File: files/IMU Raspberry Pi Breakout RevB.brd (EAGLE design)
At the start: 65 x 56 mm, 13 parts, among them J1 PIN20X2, J2 ADIS1648X/49X/54X, J4 455-1750-1-ND, U1 ADM7172ACPZ-3.3-R7

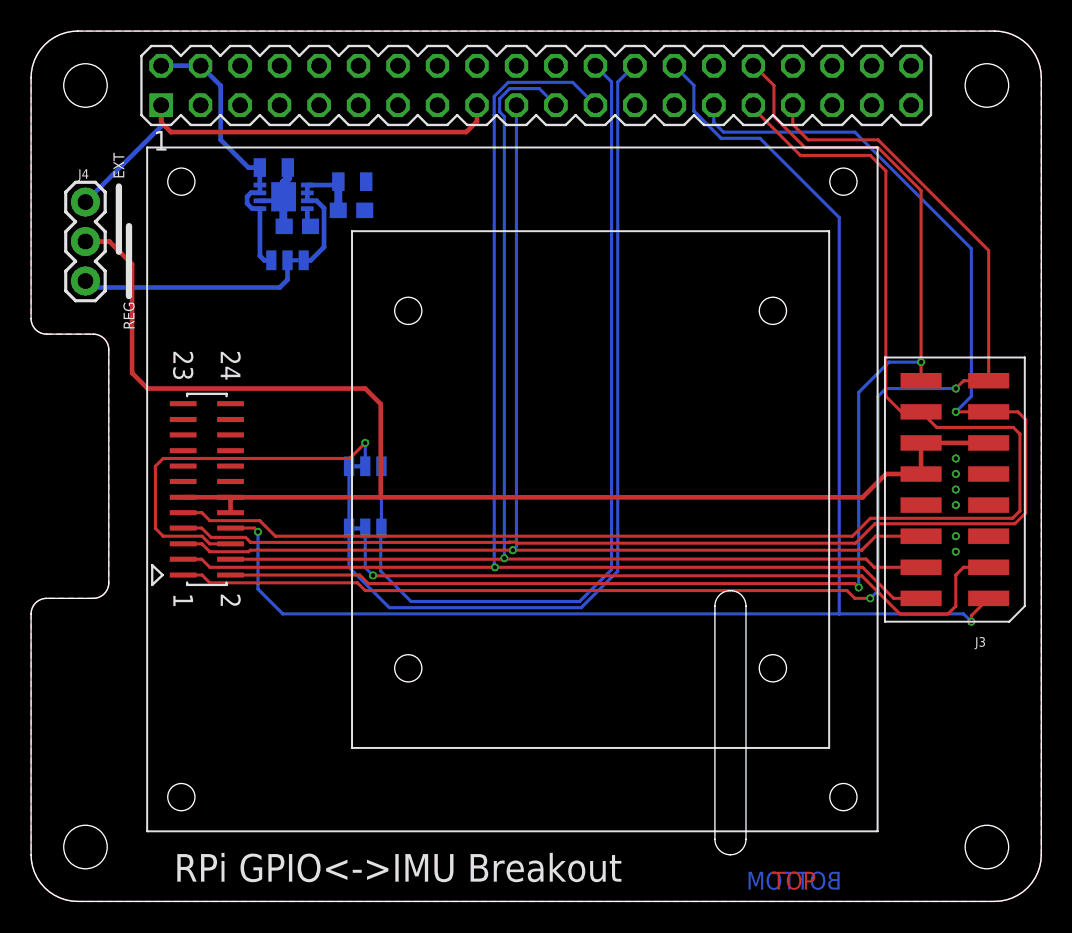
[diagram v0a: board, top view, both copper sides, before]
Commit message: Updated design to include resistors that link SPI1 to SPI0. Improved silkscreen art.
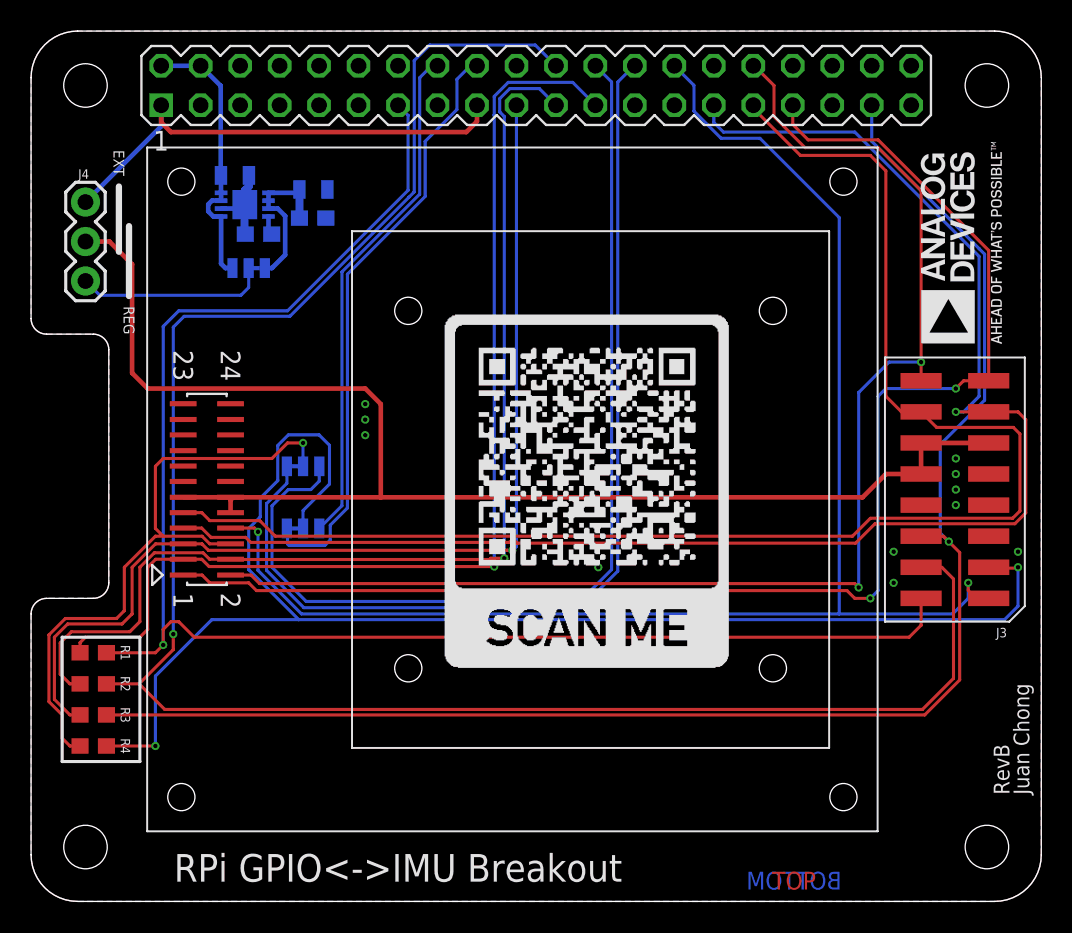
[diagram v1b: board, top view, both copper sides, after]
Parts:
- added R1, R2, R3, R4: 0, SparkFun-Resistors:0603
- moved JP1 4.00 mm to (17.5, 28.0)
- moved JP2 4.00 mm to (17.5, 24.0)
- moved U1 2.55 mm to (13.7, 44.8)
- moved C1 2.55 mm to (13.1, 46.7)
- moved C2 2.55 mm to (18.2, 45.8)
- moved C4 2.55 mm to (18.1, 44.0)
- moved JP3 2.55 mm to (14.0, 40.8)
- moved C3 2.55 mm to (14.6, 42.9)
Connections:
- removed net MISO: J1.21, J2.4, J3.4
- removed net MOSI: J1.19, J2.5, J3.6
- removed net N$2: J1.26, JP1.3, JP2.3
- removed net N$3: J1.24, JP1.1, JP2.1
- removed net SCLK: J1.23, J2.3, J3.2
- new net SPI0_CS0: J1.24, JP1.1
- new net SPI0_CS1: J1.26, JP1.3
- new net SPI0_MISO: J1.21, J2.4, R2.2
- new net SPI0_MOSI: J1.19, J2.5, R3.2
- new net SPI0_SCLK: J1.23, J2.3, R1.2
- new net SPI1_CS0: J1.18, JP2.3
- new net SPI1_CS1: J1.16, JP2.1
- new net SPI1_MISO: J1.22, J3.4, R2.1
- new net SPI1_MOSI: J1.37, J3.6, R3.1
- new net SPI1_SCLK: J1.13, J3.2, R1.1
- net !CS_1MM: now also R4.2
- net !CS_2MM: now also R4.1
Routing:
- net SPI1_MISO: track 0.00 -> 126.3 mm, vias 0 -> 1
- net SPI1_SCLK: track 0.00 -> 101.9 mm, vias 0 -> 1
- net SPI1_MOSI: track 0.00 -> 99.4 mm, vias 0 -> 1
- net SCLK: track 86.3 -> 0.00 mm, vias 1 -> 0
- net MISO: track 78.7 -> 0.00 mm, vias 1 -> 0
- net MOSI: track 76.8 -> 0.00 mm, vias 1 -> 0
- net SPI0_MISO: track 0.00 -> 70.8 mm, vias 0 -> 1
- net SPI0_SCLK: track 0.00 -> 69.8 mm, vias 0 -> 1
- net SPI0_MOSI: track 0.00 -> 68.7 mm, vias 0 -> 1
- net SPI0_CS0: track 0.00 -> 65.1 mm
- net SPI0_CS1: track 0.00 -> 64.8 mm
- net N$2: track 58.9 -> 0.00 mm
- net N$3: track 56.1 -> 0.00 mm
- net !CS_2MM: track 46.3 -> 92.8 mm, vias 1 -> 2
- net SPI1_CS0: track 0.00 -> 38.6 mm
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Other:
- outline, holes or cut-outs redrawn
- board text added: "Install R1-R4 to share SPI0 and SPI1"
